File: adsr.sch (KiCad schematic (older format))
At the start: 28 parts, among them U1 TL074, U2 7555

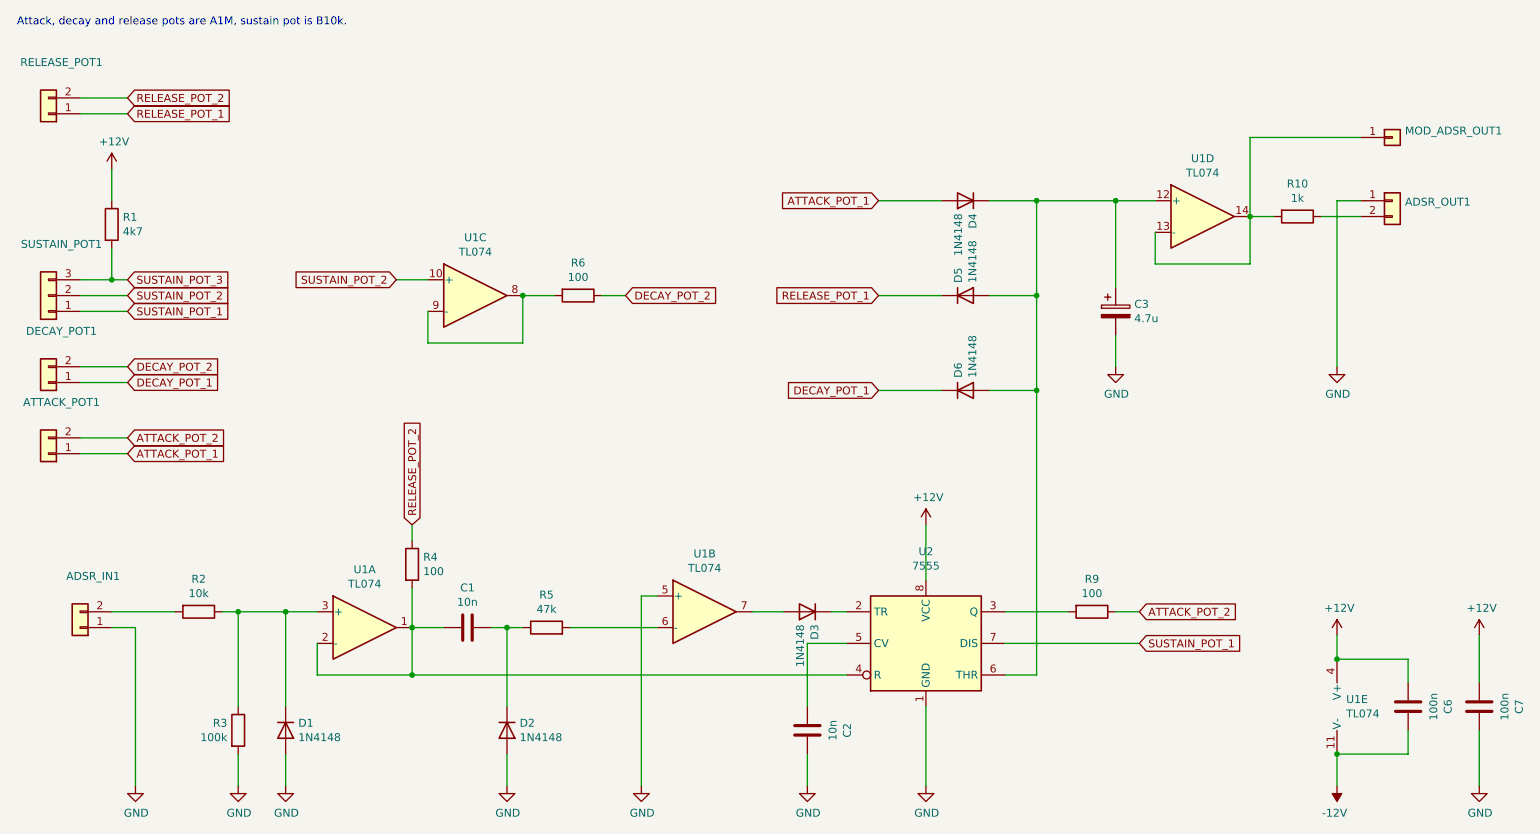
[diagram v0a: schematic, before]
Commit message: Fix envelope trigger
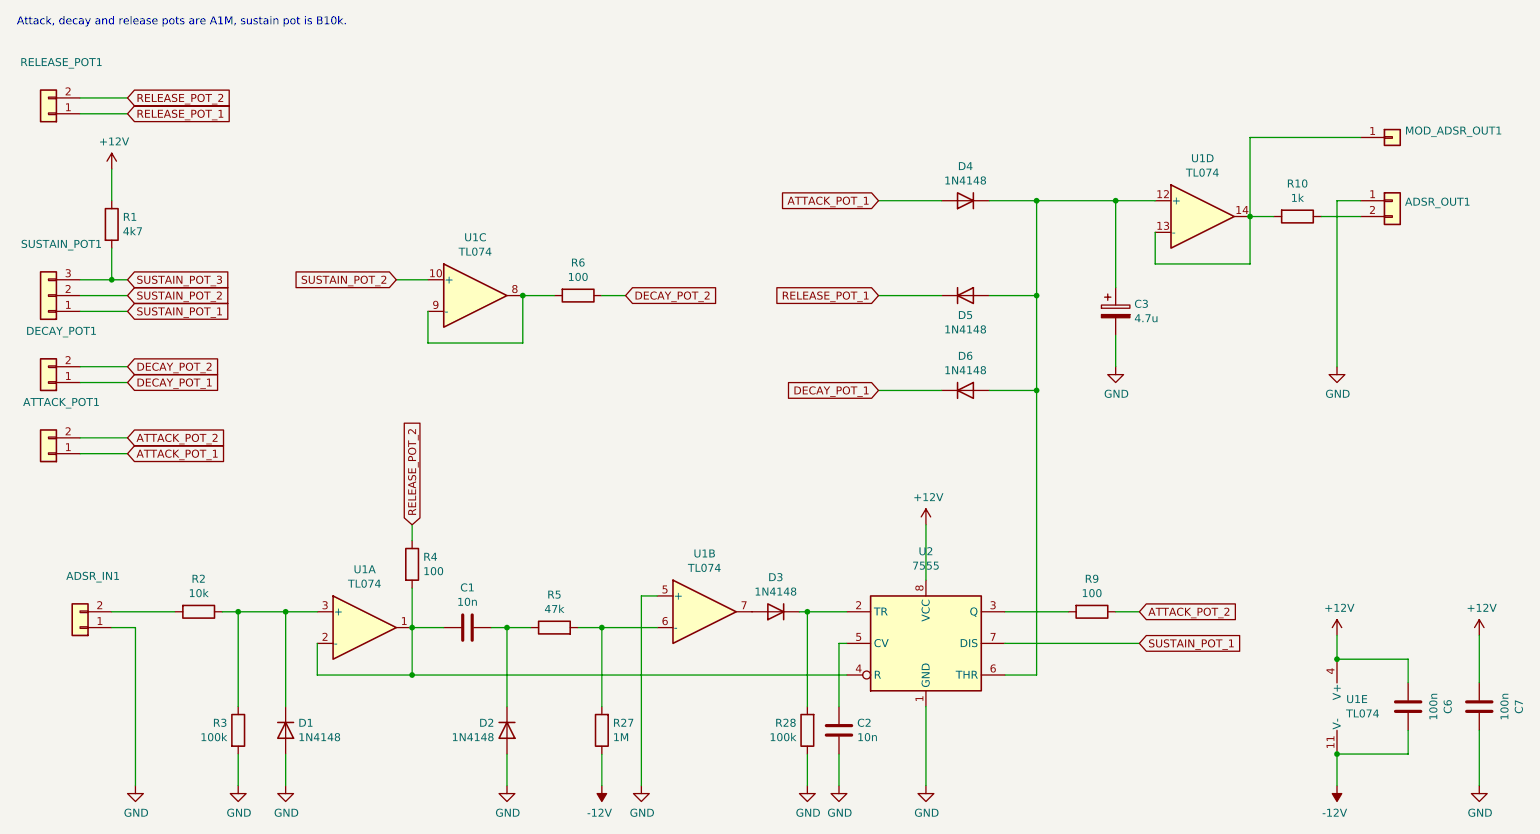
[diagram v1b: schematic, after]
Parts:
- added R27: 1M, Resistor_THT:R_Axial_DIN0207_L6.3mm_D2.5mm_P2.54mm_Vertical, symbol Device:R
- added R28: 100k, Resistor_THT:R_Axial_DIN0207_L6.3mm_D2.5mm_P2.54mm_Vertical, symbol Device:R
- R4, R5: footprint Resistor_THT:R_Axial_DIN0207_L6.3mm_D2.5mm_P7.62mm_Horizontal -> Resistor_THT:R_Axial_DIN0207_L6.3mm_D2.5mm_P2.54mm_Vertical
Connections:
- net -12V: now also R27.1
- net GND: now also R28.1
- net at R5.2, U1.6 (-): now also R27.2
- net at D3.1 (K), U2.2 (TR): now also R28.2
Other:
- moved on the sheet: C2, D3, R5
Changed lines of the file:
@@
 Title "ADSR"
 Date "2021-02-15"
-Rev "v1.0.0"
+Rev "v1.0.1"
 Comp "Jan Knipper"
 Comment1 "github.com/polykit/vca-adsr"
@@
 U 1 1 602748B0
 P 4400 5350
-F 0 "D2" V 4354 5430 50  0000 L CNN
-F 1 "1N4148" V 4445 5430 50  0000 L CNN
+F 0 "D2" V 4354 5270 50  0000 R CNN
+F 1 "1N4148" V 4445 5270 50  0000 R CNN
 F 2 "Diode_THT:D_DO-35_SOD27_P7.62mm_Horizontal" H 4400 5175 50  0001 C CNN
 F 3 "https://assets.nexperia.com/documents/data-sheet/1N4148_1N4448.pdf" H 4400 5350 50  0001 C CNN
@@
 L Device:R R5
 U 1 1 60275BCF
-P 4650 4700
-F 0 "R5" V 4857 4700 50  0000 C CNN
-F 1 "47k" V 4766 4700 50  0000 C CNN
-F 2 "Resistor_THT:R_Axial_DIN0207_L6.3mm_D2.5mm_P7.62mm_Horizontal" V 4580 4700 50  0001 C CNN
-F 3 "~" H 4650 4700 50  0001 C CNN
-	1    4650 4700
+P 4700 4700
+F 0 "R5" V 4907 4700 50  0000 C CNN
+F 1 "47k" V 4816 4700 50  0000 C CNN
+F 2 "Resistor_THT:R_Axial_DIN0207_L6.3mm_D2.5mm_P2.54mm_Vertical" V 4630 4700 50  0001 C CNN
+F 3 "~" H 4700 4700 50  0001 C CNN
+	1    4700 4700
 	0    -1   -1   0
 $EndComp
@@
 Wire Wire Line
 	4300 4700 4400 4700
-Connection ~ 4400 4700
-Wire Wire Line
-	4400 4700 4500 4700
 $Comp
 L power:GND #PWR0101
@@
 L Diode:1N4148 D3
 U 1 1 602A2BAD
-P 6300 4600
-F 0 "D3" V 6254 4680 50  0000 L CNN
-F 1 "1N4148" V 6345 4680 50  0000 L CNN
-F 2 "Diode_THT:D_DO-35_SOD27_P7.62mm_Horizontal" H 6300 4425 50  0001 C CNN
-F 3 "https://assets.nexperia.com/documents/data-sheet/1N4148_1N4448.pdf" H 6300 4600 50  0001 C CNN
-	1    6300 4600
-	-1   0    0    1
-$EndComp
-Wire Wire Line
-	6550 4600 6450 4600
-Wire Wire Line
-	6150 4600 5950 4600
+P 6100 4600
+F 0 "D3" H 6100 4383 50  0000 C CNN
+F 1 "1N4148" H 6100 4474 50  0000 C CNN
+F 2 "Diode_THT:D_DO-35_SOD27_P7.62mm_Horizontal" H 6100 4425 50  0001 C CNN
+F 3 "https://assets.nexperia.com/documents/data-sheet/1N4148_1N4448.pdf" H 6100 4600 50  0001 C CNN
+	1    6100 4600
+	-1   0    0    1
+$EndComp
 $Comp
 L Device:C C2
 U 1 1 602A5D54
-P 6300 5350
-F 0 "C2" V 6048 5350 50  0000 C CNN
-F 1 "10n" V 6139 5350 50  0000 C CNN
-F 2 "Capacitor_THT:C_Disc_D5.0mm_W2.5mm_P5.00mm" H 6338 5200 50  0001 C CNN
-F 3 "~" H 6300 5350 50  0001 C CNN
-	1    6300 5350
+P 6500 5350
+F 0 "C2" H 6385 5304 50  0000 R CNN
+F 1 "10n" H 6385 5395 50  0000 R CNN
+F 2 "Capacitor_THT:C_Disc_D5.0mm_W2.5mm_P5.00mm" H 6538 5200 50  0001 C CNN
+F 3 "~" H 6500 5350 50  0001 C CNN
+	1    6500 5350
 	-1   0    0    1
 $EndComp
@@
 L power:GND #PWR0106
 U 1 1 602A6D46
-P 6300 5700
-F 0 "#PWR0106" H 6300 5450 50  0001 C CNN
-F 1 "GND" H 6305 5527 50  0000 C CNN
-F 2 "" H 6300 5700 50  0001 C CNN
-F 3 "" H 6300 5700 50  0001 C CNN
-	1    6300 5700
-	1    0    0    -1
-$EndComp
-Wire Wire Line
-	6300 5700 6300 5500
-Wire Wire Line
-	6550 4800 6300 4800
-Wire Wire Line
-	6300 4800 6300 5200
+P 6500 5700
+F 0 "#PWR0106" H 6500 5450 50  0001 C CNN
+F 1 "GND" H 6505 5527 50  0000 C CNN
+F 2 "" H 6500 5700 50  0001 C CNN
+F 3 "" H 6500 5700 50  0001 C CNN
+	1    6500 5700
+	1    0    0    -1
+$EndComp
+Wire Wire Line
+	6500 5700 6500 5500
 $Comp
 L power:GND #PWR0107
@@
 U 1 1 602DC291
 P 7300 2000
-F 0 "D4" V 7254 2080 50  0000 L CNN
-F 1 "1N4148" V 7345 2080 50  0000 L CNN
+F 0 "D4" H 7300 1783 50  0000 C CNN
+F 1 "1N4148" H 7300 1874 50  0000 C CNN
 F 2 "Diode_THT:D_DO-35_SOD27_P7.62mm_Horizontal" H 7300 1825 50  0001 C CNN
 F 3 "https://assets.nexperia.com/documents/data-sheet/1N4148_1N4448.pdf" H 7300 2000 50  0001 C CNN
@@
 U 1 1 603078AE
 P 7300 2600
-F 0 "D5" V 7254 2680 50  0000 L CNN
-F 1 "1N4148" V 7345 2680 50  0000 L CNN
+F 0 "D5" H 7300 2475 50  0000 C CNN
+F 1 "1N4148" H 7300 2384 50  0000 C CNN
 F 2 "Diode_THT:D_DO-35_SOD27_P7.62mm_Horizontal" H 7300 2425 50  0001 C CNN
 F 3 "https://assets.nexperia.com/documents/data-sheet/1N4148_1N4448.pdf" H 7300 2600 50  0001 C CNN
@@
 U 1 1 60309859
 P 7300 3200
-F 0 "D6" V 7254 3280 50  0000 L CNN
-F 1 "1N4148" V 7345 3280 50  0000 L CNN
+F 0 "D6" H 7300 3417 50  0000 C CNN
+F 1 "1N4148" H 7300 3326 50  0000 C CNN
 F 2 "Diode_THT:D_DO-35_SOD27_P7.62mm_Horizontal" H 7300 3025 50  0001 C CNN
 F 3 "https://assets.nexperia.com/documents/data-sheet/1N4148_1N4448.pdf" H 7300 3200 50  0001 C CNN
@@
 F 0 "R4" H 3870 4346 50  0000 L CNN
 F 1 "100" H 3870 4255 50  0000 L CNN
-F 2 "Resistor_THT:R_Axial_DIN0207_L6.3mm_D2.5mm_P7.62mm_Horizontal" V 3730 4300 50  0001 C CNN
+F 2 "Resistor_THT:R_Axial_DIN0207_L6.3mm_D2.5mm_P2.54mm_Vertical" V 3730 4300 50  0001 C CNN
 F 3 "~" H 3800 4300 50  0001 C CNN
 	1    3800 4300
@@
 $EndComp
 Wire Wire Line
-	4800 4700 5350 4700
-Wire Wire Line
 	4400 4700 4400 5200
 Wire Wire Line
@@
 Wire Wire Line
 	9100 1600 9100 2100
+$Comp
+L Device:R R27
+U 1 1 6136D5C5
+P 5000 5350
+F 0 "R27" H 4930 5304 50  0000 R CNN
+F 1 "1M" H 4930 5395 50  0000 R CNN
+F 2 "Resistor_THT:R_Axial_DIN0207_L6.3mm_D2.5mm_P2.54mm_Vertical" V 4930 5350 50  0001 C CNN
+F 3 "~" H 5000 5350 50  0001 C CNN
+	1    5000 5350
+	-1   0    0    1
+$EndComp
+Wire Wire Line
+	5000 5700 5000 5500
+Wire Wire Line
+	5000 5200 5000 4700
+Wire Wire Line
+	6550 4800 6500 4800
+Wire Wire Line
+	6500 4800 6500 5200
+$Comp
+L Device:R R28
+U 1 1 61396FC5
+P 6300 5350
+F 0 "R28" H 6369 5304 50  0000 L CNN
+F 1 "100k" H 6369 5395 50  0000 L CNN
+F 2 "Resistor_THT:R_Axial_DIN0207_L6.3mm_D2.5mm_P2.54mm_Vertical" V 6230 5350 50  0001 C CNN
+F 3 "~" H 6300 5350 50  0001 C CNN
+	1    6300 5350
+	-1   0    0    1
+$EndComp
+Wire Wire Line
+	6300 5200 6300 4600
+Wire Wire Line
+	6300 4600 6250 4600
+Wire Wire Line
+	6550 4600 6300 4600
+Connection ~ 6300 4600
+$Comp
+L power:GND #PWR0132
+U 1 1 6139EED8
+P 6300 5700
+F 0 "#PWR0132" H 6300 5450 50  0001 C CNN
+F 1 "GND" H 6305 5527 50  0000 C CNN
+F 2 "" H 6300 5700 50  0001 C CNN
+F 3 "" H 6300 5700 50  0001 C CNN
+	1    6300 5700
+	1    0    0    -1
+$EndComp
+Wire Wire Line
+	6300 5700 6300 5500
+$Comp
+L power:-12V #PWR0133
+U 1 1 613A46A4
+P 5000 5700
+F 0 "#PWR0133" H 5000 5800 50  0001 C CNN
+F 1 "-12V" H 5015 5873 50  0000 C CNN
+F 2 "" H 5000 5700 50  0001 C CNN
+F 3 "" H 5000 5700 50  0001 C CNN
+	1    5000 5700
+	-1   0    0    1
+$EndComp
+Wire Wire Line
+	4550 4700 4400 4700
+Connection ~ 4400 4700
+Wire Wire Line
+	4850 4700 5000 4700
+Connection ~ 5000 4700
+Wire Wire Line
+	5000 4700 5350 4700
 $EndSCHEMATC
